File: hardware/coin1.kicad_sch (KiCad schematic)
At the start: 27 parts, among them J1 Conn_01x04, J2 Conn_01x03, U1 WCH CH32V003F4U6

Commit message: add LCSC part details
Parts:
- D1, D10, D2, D3, D4, D5, D6, D7, D8, D9: LCSC (none) -> C3646923
- R1, R10, R2, R3, R4, R5, R6, R7, R8, R9: value R -> 47R; LCSC (none) -> C620443
- U1: LCSC (none) -> C5299908

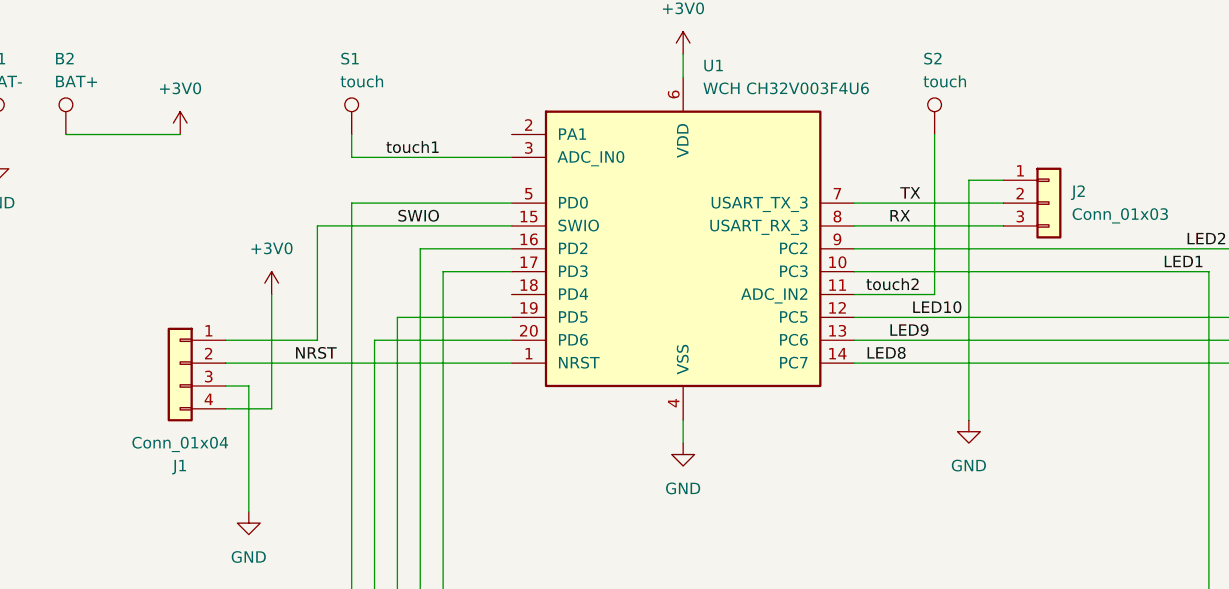
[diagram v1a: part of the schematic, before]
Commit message: use pin headers for their pads only
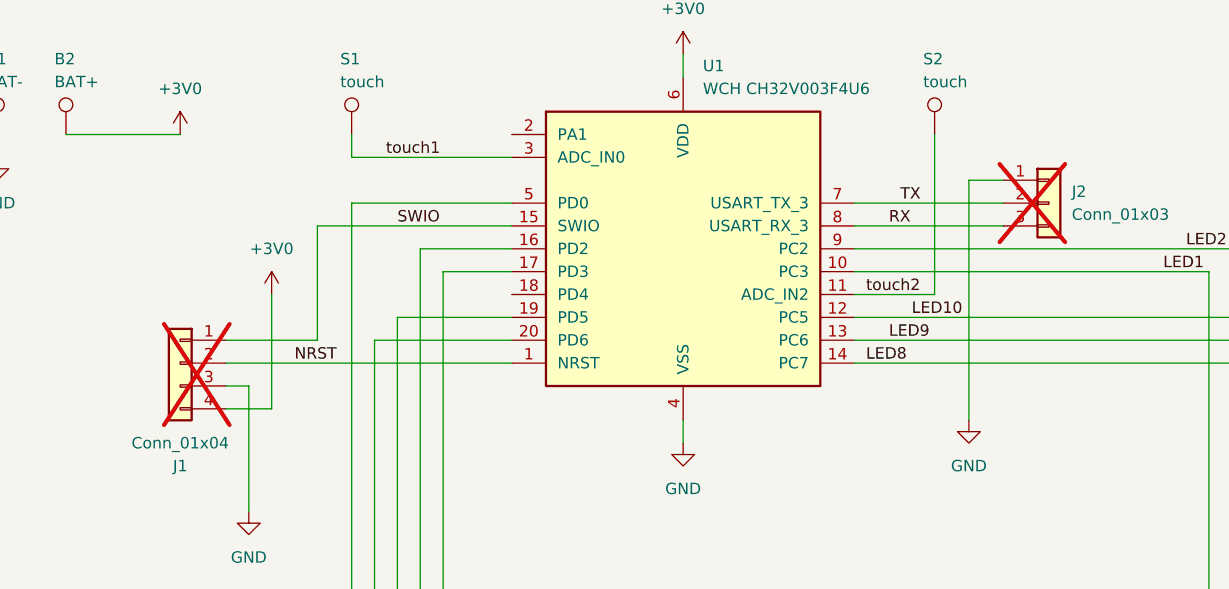
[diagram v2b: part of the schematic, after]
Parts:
- J1, J2: now not fitted; now left out of the parts list
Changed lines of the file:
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@@
 		(unit 1)
 		(exclude_from_sim no)
-		(in_bom yes)
-		(on_board yes)
-		(dnp no)
+		(in_bom no)
+		(on_board yes)
+		(dnp yes)
 		(property "Reference" "J1"
 			(at 52.07 86.36 0)
@@
 		(unit 1)
 		(exclude_from_sim no)
-		(in_bom yes)
-		(on_board yes)
-		(dnp no)
+		(in_bom no)
+		(on_board yes)
+		(dnp yes)
 		(fields_autoplaced yes)
 		(property "Reference" "J2"
